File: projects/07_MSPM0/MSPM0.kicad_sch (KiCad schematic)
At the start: 36 parts, among them J1 USB_C_Receptacle_USB2.0_16P, J2 Conn_ARM_SWD_TagConnect_TC2030, U1 MSPM0G3507SPTR, U3 SPX3819M5-L-3-3, U4 CH340E, U5 LSM6DSR, U7 MMC5983MA, Y1 8MHz

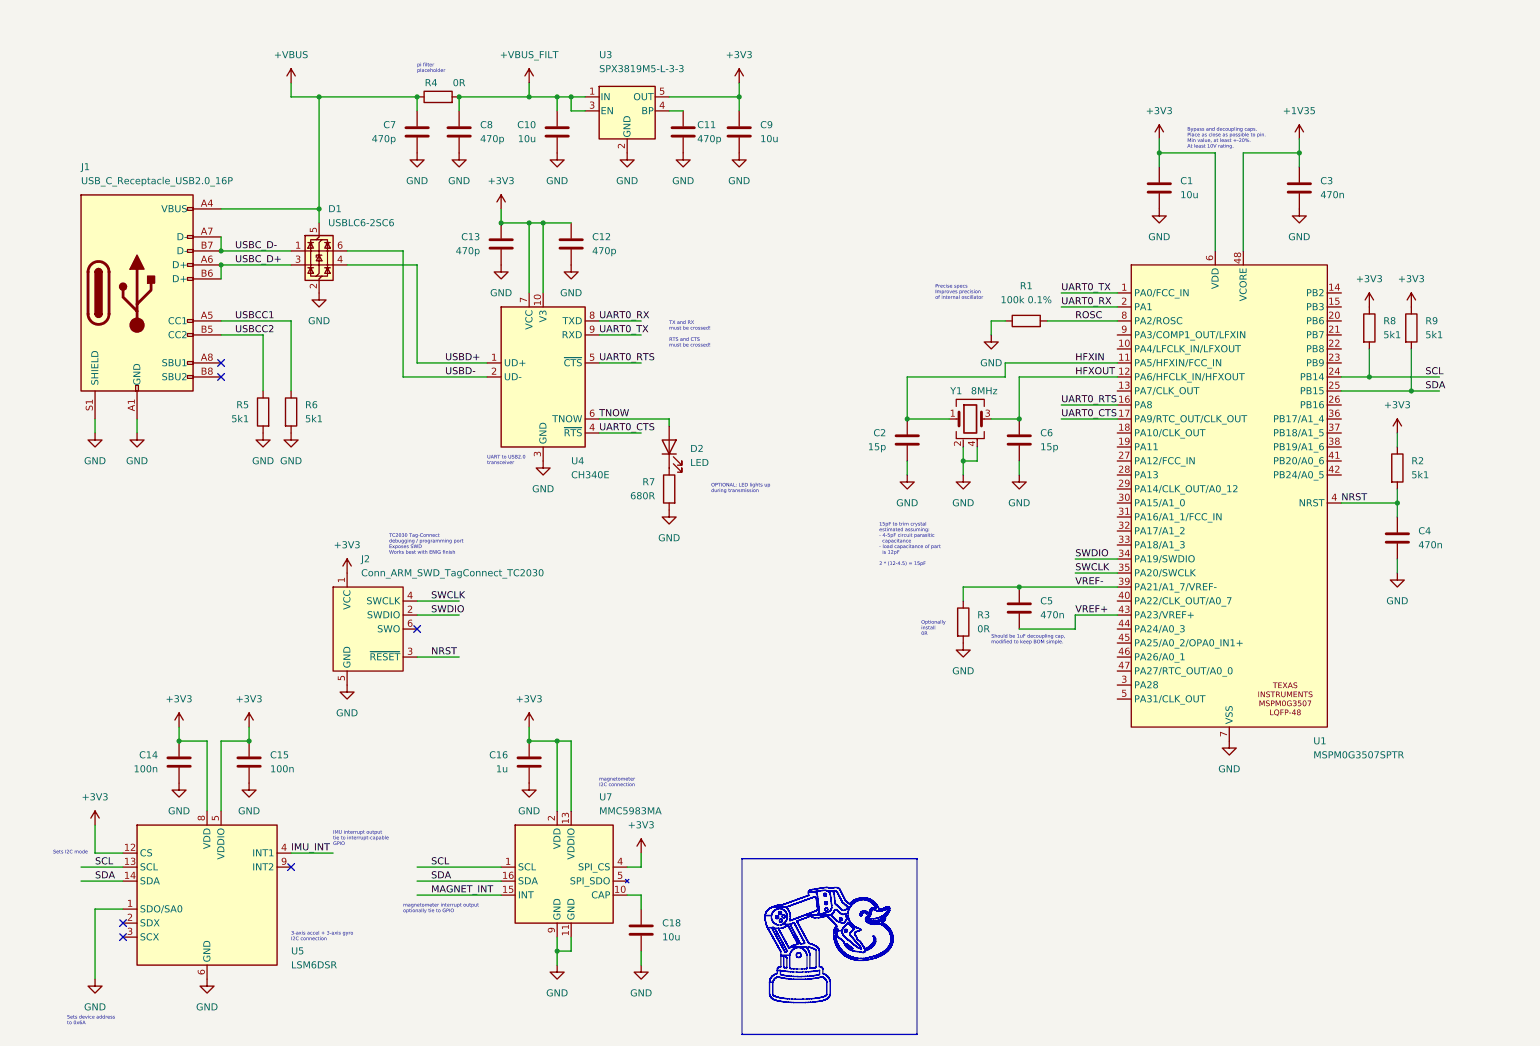
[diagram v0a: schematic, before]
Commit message: MSPM0 - migrate to KiCad 10, clean up schematic
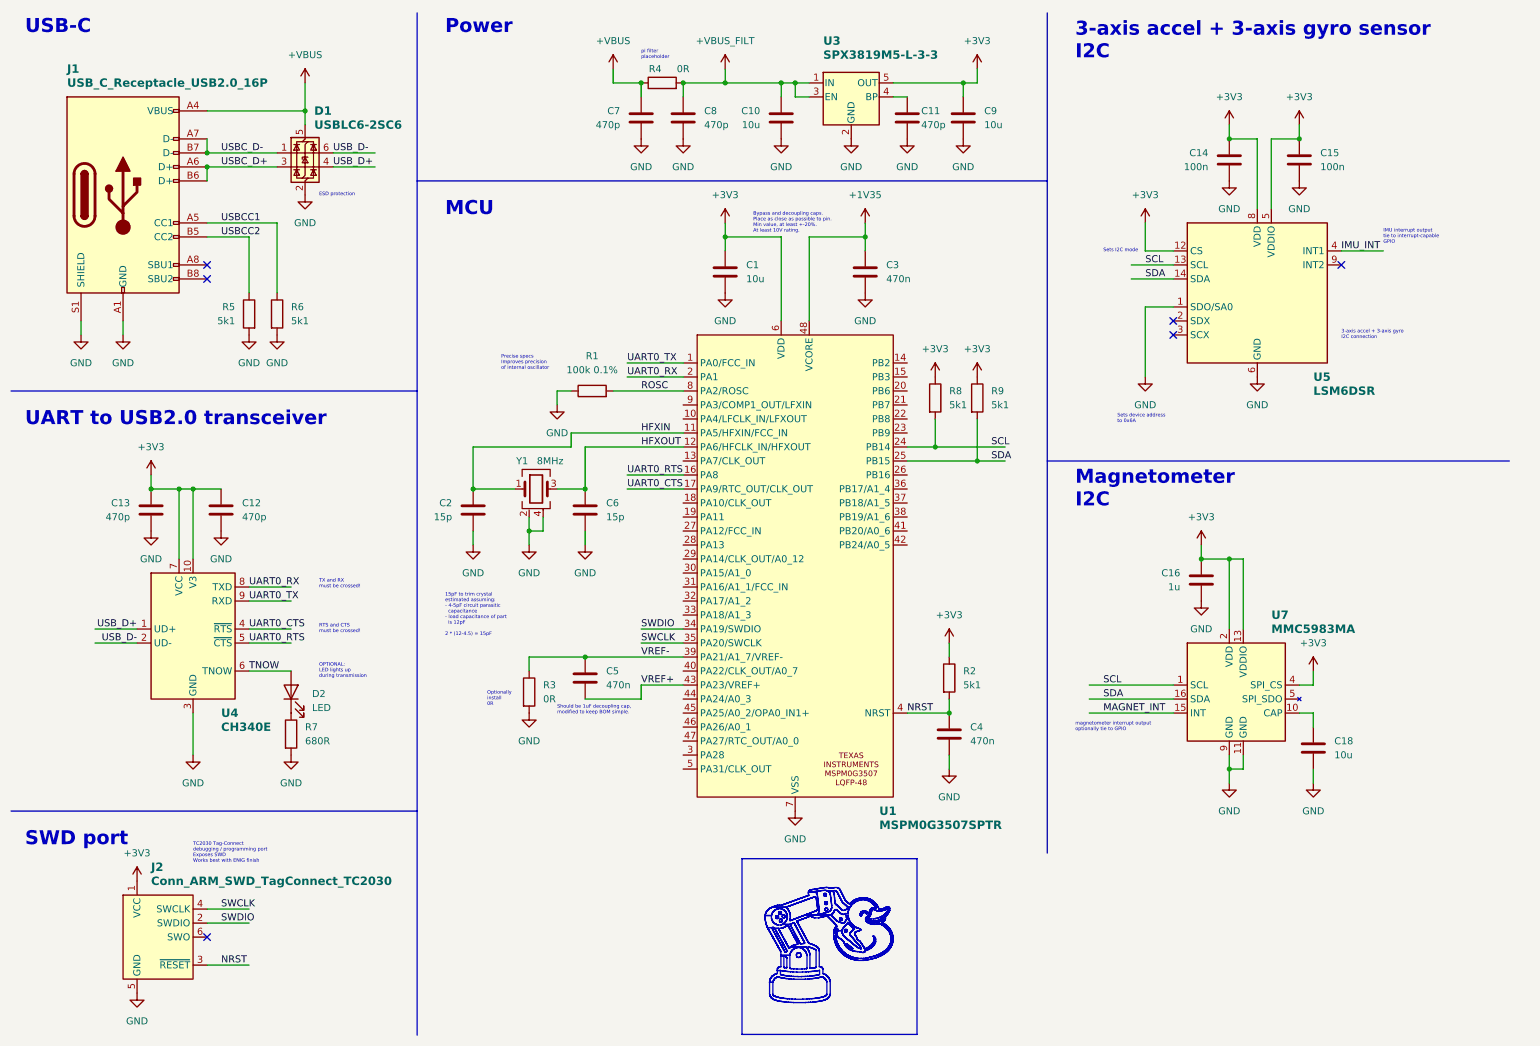
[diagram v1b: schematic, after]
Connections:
- net USBD+ renamed USB_D+
- net USBD- renamed USB_D-
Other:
- note added: "3-axis accel + 3-axis gyro sensor I2C"
- note added: "ESD protection"
- note added: "MCU"
- note added: "Magnetometer I2C"
- note added: "Power"
- note added: "RTS and CTS must be crossed!"
- note added: "SWD port"
- note added: "TX and RX must be crossed!"
- note added: "USB-C"
- note removed: "TX and RX must be crossed! RTS and CTS must be crossed!"
- note removed: "magnetometer I2C connection"
- moved on the sheet: C1, C10, C11, C12, C13, C14, C15, C16, C18, C2, C3, C4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

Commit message: MSPM0 - Complete schematic, pass ERC checks, import footprints to PCB.
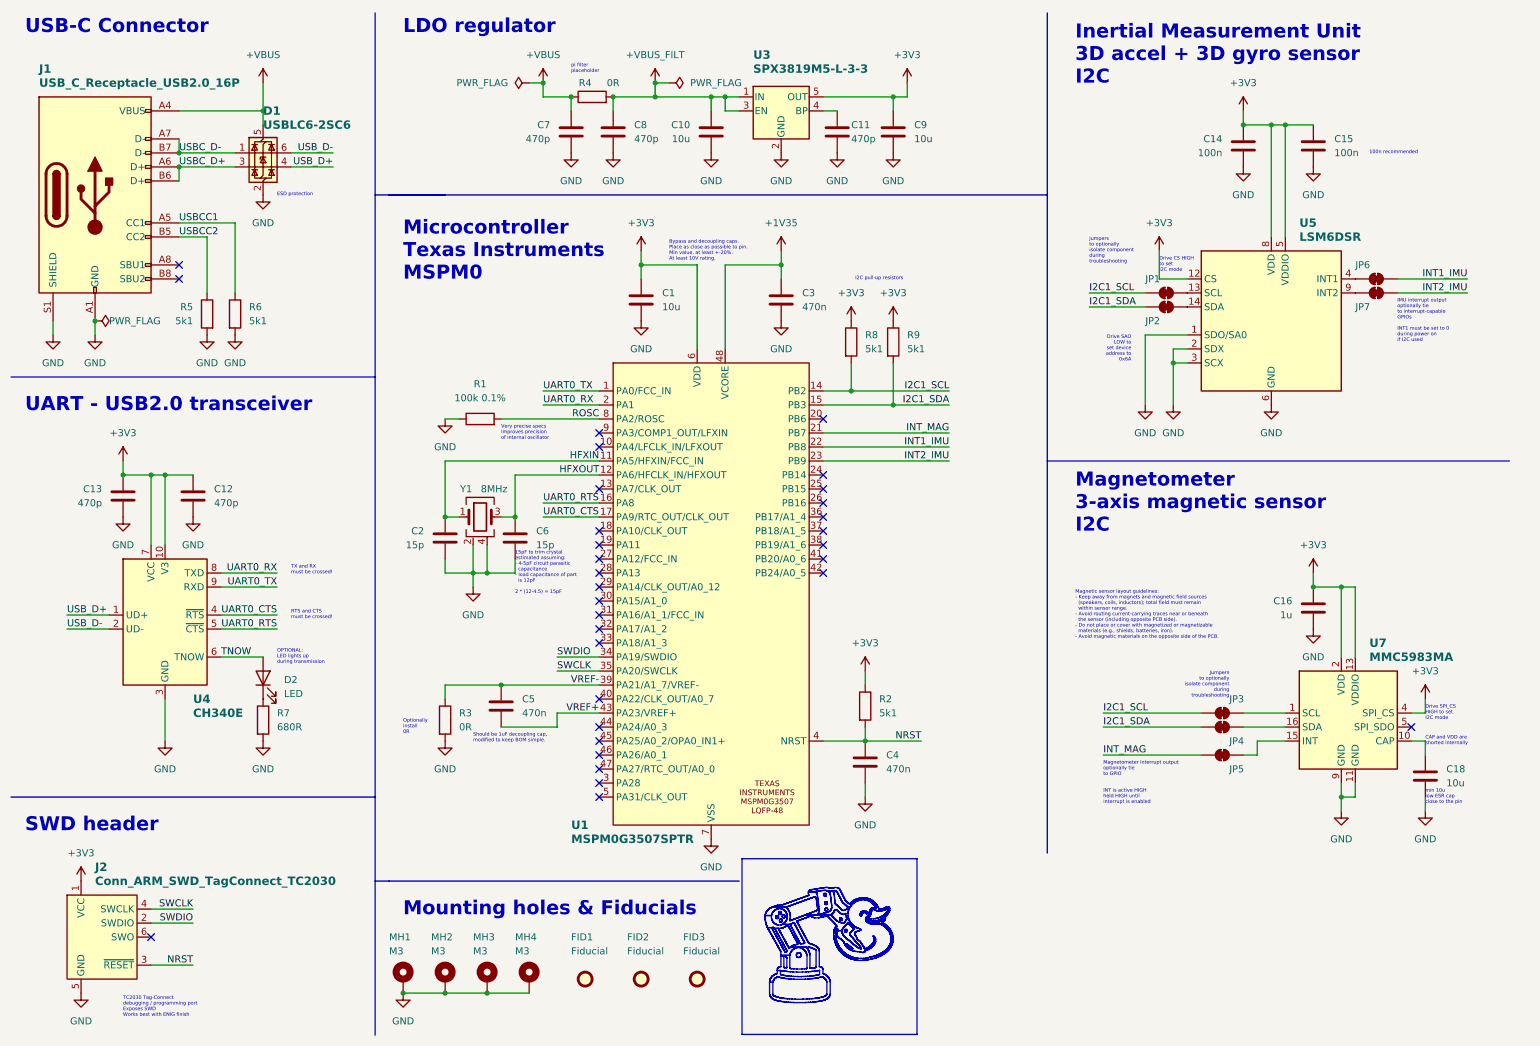
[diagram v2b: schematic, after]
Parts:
- added FID1, FID2, FID3: Fiducial, Fiducial:Fiducial_1mm_Mask2mm, symbol Mechanical:Fiducial
- added JP1, JP2, JP3, JP4, JP5, JP6, JP7: SolderJumper_2_Bridged, Jumper:SolderJumper-2_P1.3mm_Bridged_RoundedPad1.0x1.5mm, symbol MH_library:SolderJumper_2_Bridged
- added MH1, MH2, MH3, MH4: M3, MountingHole:MountingHole_3.2mm_M3_Pad_Via, symbol Mechanical:MountingHole_Pad
- C11, C12, C13, C14, C15, C2, C3, C4, C5, C6, C7, C8: footprint Capacitor_SMD:C_1206_3216Metric_Pad1.33x1.80mm_HandSolder -> Capacitor_SMD:C_0603_1608Metric_Pad1.08x0.95mm_HandSolder
- D1: footprint Package_TO_SOT_SMD:SOT-23-6 -> Package_TO_SOT_SMD:SOT-23-6_Handsoldering
- R1, R2, R3, R4, R5, R6, R7, R8, R9: footprint Resistor_SMD:R_0201_0603Metric_Pad0.64x0.40mm_HandSolder -> Resistor_SMD:R_0603_1608Metric_Pad0.98x0.95mm_HandSolder
- U3: footprint Package_TO_SOT_SMD:SOT-23-5 -> Package_TO_SOT_SMD:SOT-23-5_HandSoldering
- Y1: footprint Crystal:Crystal_SMD_3225-4Pin_3.2x2.5mm -> Crystal:Crystal_SMD_3225-4Pin_3.2x2.5mm_HandSoldering
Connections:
- net GND: now also U5.2 (SDX), U5.3 (SCX), MH1.1, MH2.1, MH3.1, MH4.1
- net at U5.9 (INT2): now also JP7.1 (A)
- net I2C1_SCL: now reaches U1.14 (PB2)
- net I2C1_SCL: now also R8.2, JP1.1 (A), JP3.1 (A)
- net I2C1_SDA: now reaches U1.15 (PB3)
- net I2C1_SDA: now also R9.2, JP2.1 (A), JP4.1 (A)
- net INT_MAG: now reaches U1.21 (PB7)
- net INT_MAG: now also JP5.1 (A)
- net INT1_IMU: now reaches U1.22 (PB8)
- net INT1_IMU: now also JP6.2 (B)
- net INT2_IMU: now reaches U1.23 (PB9)
- net INT2_IMU: now also JP7.2 (B)
- net IMU_INT: no longer names the net of U5.4 (INT1)
- net IMU_INT: now also JP6.1 (A)
- net MAGNET_INT: no longer names the net of U7.15 (INT)
- net MAGNET_INT: now also JP5.2 (B)
- removed net SCL: R8.2, U1.24 (PB14), U5.13 (SCL), U7.1 (SCL)
- removed net SDA: R9.2, U1.25 (PB15), U5.14 (SDA), U7.16 (SDA)
- new net: JP1.2 (B), U5.13 (SCL)
- new net: JP2.2 (B), U5.14 (SDA)
- new net: JP4.2 (B), U7.16 (SDA)
- new net: JP3.2 (B), U7.1 (SCL)
- no-connect marks 6 -> 32
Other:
- note added: "100n recommended"
- note added: "CAP and VDD are shorted internally"
- note added: "Drive CS HIGH to set I2C mode"
- note added: "Drive SAO LOW to set device address to 0x6A"
- note added: "Drive SPI_CS HIGH to set I2C mode"
- note added: "I2C pull-up resistors"
- note added: "IMU interrupt output optionally tie to interrupt-capable GPIOs INT1 must be set to 0 during power on if I2C used"
- note added: "INT is active HIGH held HIGH until interrupt is enabled"
- note added: "Inertial Measurement Unit 3D accel + 3D gyro sensor I2C"
- note added: "Jumpers to optionally isolate component during troubleshooting"
- note added: "LDO regulator"
- note added: "Magnetic sensor layout guidelines: - Keep away from magnets and magnetic field sources (speakers, coils, inductors); total field must remain within sensor range. - Avoid routing current-carrying traces near or beneath the sensor (including opposite PCB side). - Do not place or cover with magnetized or magnetizable materials (e.g., shields, batteries, iron). - Avoid magnetic materials on the oppos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"
- note added: "Magnetometer 3-axis magnetic sensor I2C"
- note added: "Magnetometer interrupt output optionally tie to GPIO"
- note added: "Microcontroller Texas Instruments MSPM0"
- note added: "Mounting holes & Fiducials"
- note added: "SWD header"
- note added: "UART - USB2.0 transceiver"
- note added: "USB-C Connector"
- note added: "Very precise specs Improves precision of internal oscillator"
- note added: "min 10u low ESR cap close to the pin"
- note removed: "3-axis accel + 3-axis gyro I2C connection"
- note removed: "3-axis accel + 3-axis gyro sensor I2C"
- note removed: "IMU interrupt output tie to interrupt-capable GPIO"
- note removed: "MCU"
- note removed: "Magnetometer I2C"
- note removed: "Power"
- note removed: "Precise specs Improves precision of internal oscillator"
- note removed: "SWD port"
- note removed: "Sets I2C mode"
- note removed: "Sets device address to 0x6A"
- note removed: "UART to USB2.0 transceiver"
- note removed: "USB-C"
- note removed: "magnetometer interrupt output optionally tie to GPIO"
- moved on the sheet: C1, C10, C11, C12, C13, C14, C15, C16, C18, C2, C3, C4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

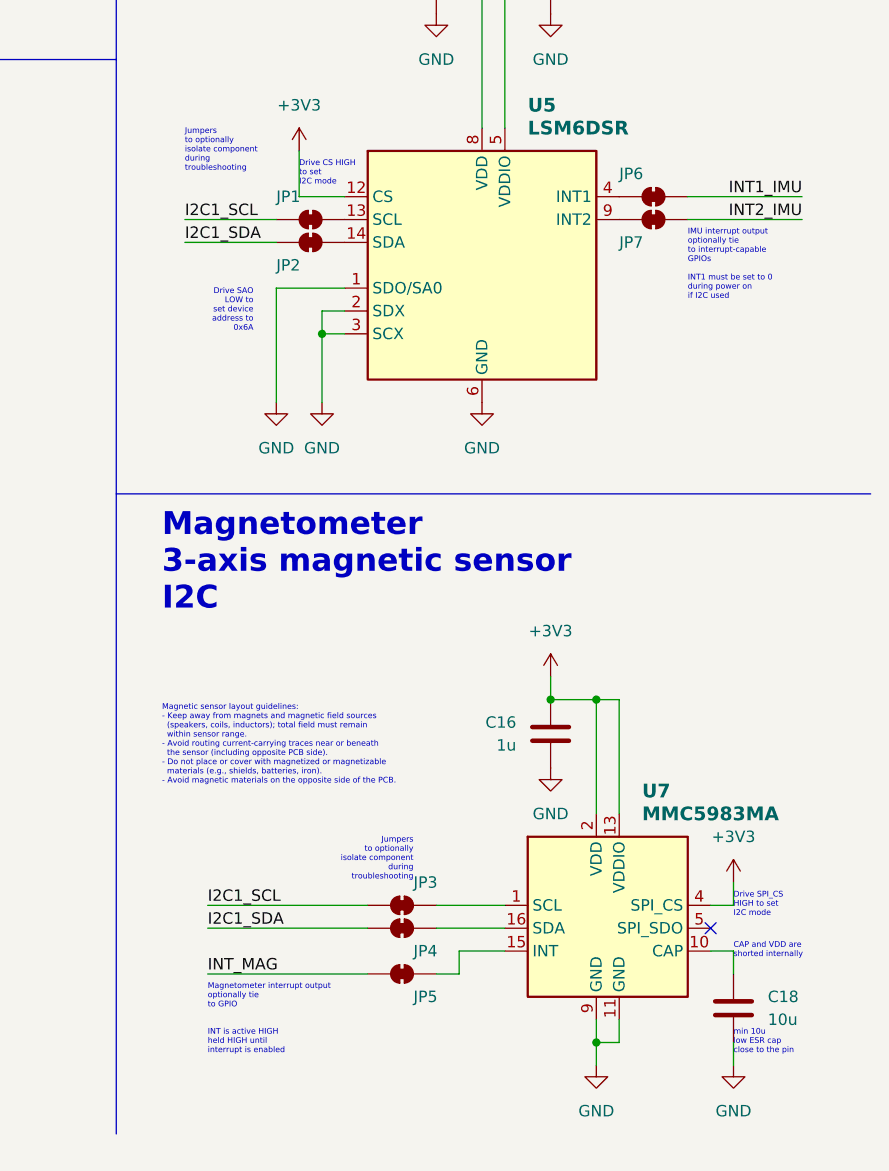
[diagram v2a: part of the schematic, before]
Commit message: MSPM0 - initialize PCB layout
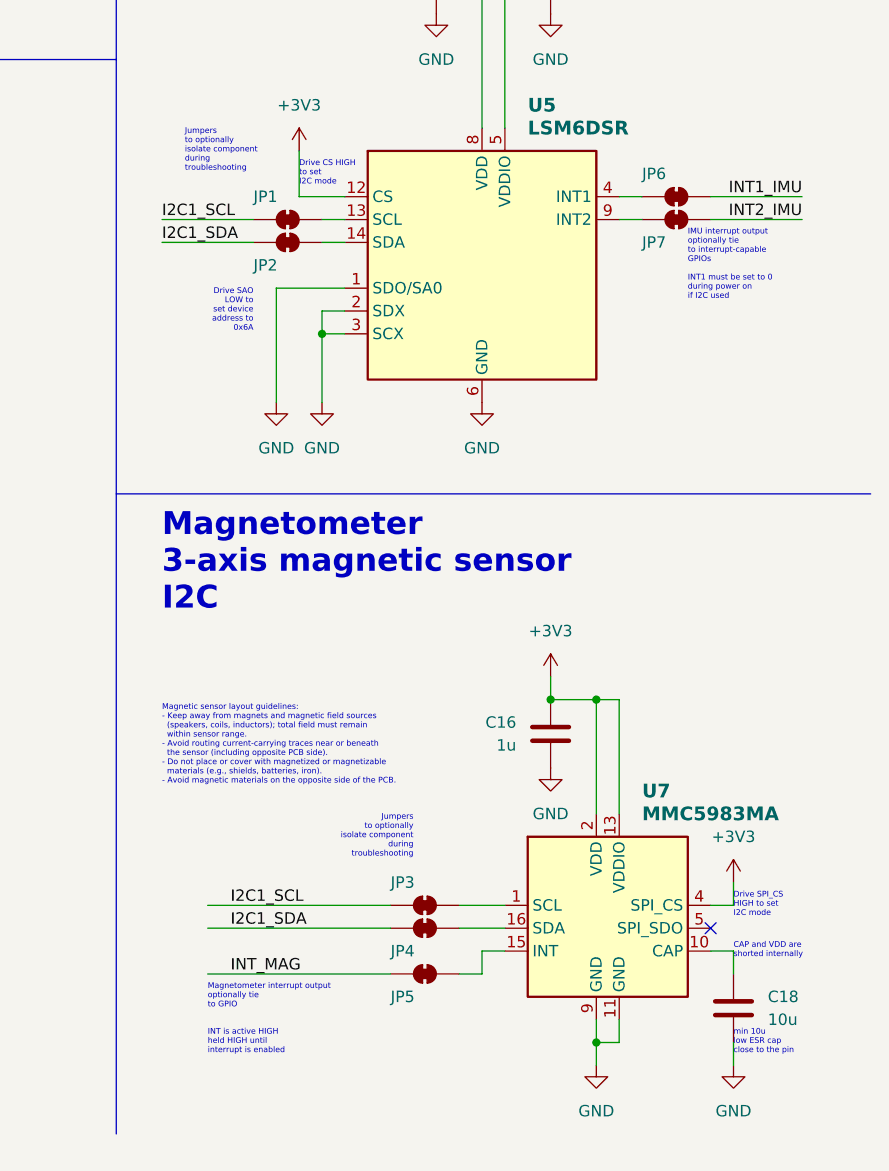
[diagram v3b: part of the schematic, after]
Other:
- moved on the sheet: JP1, JP2, JP3, JP4, JP5, JP6, JP7
